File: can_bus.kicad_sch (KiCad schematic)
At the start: 1 part, among them U8 MCP2562-E-SN

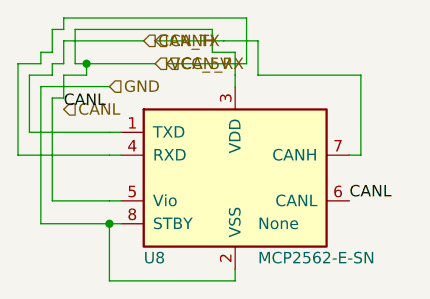
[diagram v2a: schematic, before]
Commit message: optimazed load to kicad
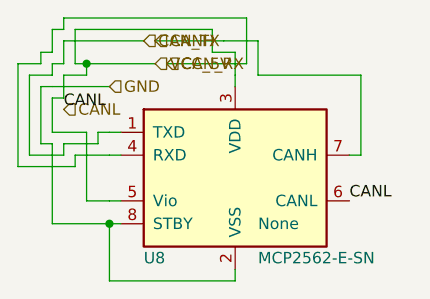
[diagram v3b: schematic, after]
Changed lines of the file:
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@@
 		(instances
 			(project "Untitled"
-				(path "/64cf9334-2063-4cd7-ba0e-d205787c78fb"
+				(path "/deb6734f-8716-41b1-a872-d87713bf0c81"
 					(reference "U8")
 					(unit 1)
@@
 	(wire
 		(pts
-			(xy 21.59 26.67) (xy 15.24 26.67)
-		)
-		(stroke
-			(width 0)
-			(type default)
-		)
-	)
-	(wire
-		(pts
-			(xy 15.24 26.67) (xy 15.24 15.24)
+			(xy 21.59 26.67) (xy 19.05 26.67)
+		)
+		(stroke
+			(width 0)
+			(type default)
+		)
+	)
+	(wire
+		(pts
+			(xy 19.05 26.67) (xy 19.05 19.05)
+		)
+		(stroke
+			(width 0)
+			(type default)
+		)
+	)
+	(wire
+		(pts
+			(xy 19.05 19.05) (xy 15.24 19.05)
+		)
+		(stroke
+			(width 0)
+			(type default)
+		)
+	)
+	(wire
+		(pts
+			(xy 15.24 19.05) (xy 15.24 15.24)
 		)
 		(stroke
@@
 	(wire
 		(pts
-			(xy 21.59 29.21) (xy 13.97 29.21)
-		)
-		(stroke
-			(width 0)
-			(type default)
-		)
-	)
-	(wire
-		(pts
-			(xy 13.97 29.21) (xy 13.97 13.97)
+			(xy 21.59 29.21) (xy 15.24 29.21)
+		)
+		(stroke
+			(width 0)
+			(type default)
+		)
+	)
+	(wire
+		(pts
+			(xy 15.24 29.21) (xy 15.24 20.32)
+		)
+		(stroke
+			(width 0)
+			(type default)
+		)
+	)
+	(wire
+		(pts
+			(xy 15.24 20.32) (xy 13.97 20.32)
+		)
+		(stroke
+			(width 0)
+			(type default)
+		)
+	)
+	(wire
+		(pts
+			(xy 13.97 20.32) (xy 13.97 13.97)
 		)
 		(stroke
@@
 	(wire
 		(pts
-			(xy 21.59 19.05) (xy 12.7 19.05)
-		)
-		(stroke
-			(width 0)
-			(type default)
-		)
-	)
-	(wire
-		(pts
-			(xy 12.7 19.05) (xy 12.7 12.7)
+			(xy 21.59 19.05) (xy 20.32 19.05)
+		)
+		(stroke
+			(width 0)
+			(type default)
+		)
+	)
+	(wire
+		(pts
+			(xy 20.32 19.05) (xy 20.32 20.32)
+		)
+		(stroke
+			(width 0)
+			(type default)
+		)
+	)
+	(wire
+		(pts
+			(xy 20.32 20.32) (xy 16.51 20.32)
+		)
+		(stroke
+			(width 0)
+			(type default)
+		)
+	)
+	(wire
+		(pts
+			(xy 16.51 20.32) (xy 16.51 21.59)
+		)
+		(stroke
+			(width 0)
+			(type default)
+		)
+	)
+	(wire
+		(pts
+			(xy 16.51 21.59) (xy 12.7 21.59)
+		)
+		(stroke
+			(width 0)
+			(type default)
+		)
+	)
+	(wire
+		(pts
+			(xy 12.7 21.59) (xy 12.7 12.7)
 		)
 		(stroke
@@
 	(wire
 		(pts
-			(xy 21.59 21.59) (xy 11.43 21.59)
-		)
-		(stroke
-			(width 0)
-			(type default)
-		)
-	)
-	(wire
-		(pts
-			(xy 11.43 21.59) (xy 11.43 11.43)
-		)
-		(stroke
+			(xy 21.59 21.59) (xy 17.78 21.59)
+		)
+		(stroke
+			(width 0)
+			(type default)
+		)
+	)
+	(wire
+		(pts
+			(xy 17.78 21.59) (xy 17.78 22.86)
+		)
+		(stroke
+			(width 0)
+			(type default)
+		)
+	)
+	(wire
+		(pts
+			(xy 17.78 22.86) (xy 11.43 22.86)
+		)
+		(stroke
+			(width 0)
+			(type default)
+		)
+	)
+	(wire
+		(pts
+			(xy 11.43 22.86) (xy 11.43 11.43)
+		)
+		(stroke

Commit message: tests_fix
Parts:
- U8: hierarchy_path (none) -> /c5a034c1-1f54-4e7e-8711-0930d2b4314e/3e6f426e-0825-4ec4-9e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
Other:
- title: (none) -> climate_control_niva_travel
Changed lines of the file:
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@@
 	(generator_version "9.0")
 	(paper "A4")
+	(title_block
+		(title "climate_control_niva_travel")
+	)
 	(symbol
 		(lib_id "Interface_CAN_LIN:MCP2562-E-SN")
@@
 			)
 		)
+		(property "hierarchy_path" "/c5a034c1-1f54-4e7e-8711-0930d2b4314e/3e6f426e-0825-4ec4-9e13-95c41a6eab89"
+			(at 38.1 29.2099 0)
+			(effects
+				(font
+					(size 1.27 1.27)
+				)
+				(justify left)
+			)
+		)
 		(pin "1"
 		)
@@
 		)
 		(instances
-			(project "Untitled"
-				(path "/deb6734f-8716-41b1-a872-d87713bf0c81"
+			(project "climate_control_niva_travel"
+				(path "/c5a034c1-1f54-4e7e-8711-0930d2b4314e/3e6f426e-0825-4ec4-9e13-95c41a6eab89"
 					(reference "U8")
 					(unit 1)
@@
 	)
 	(hierarchical_label "CAN_RX"
-		(shape input)
+		(shape output)
 		(at 27.94 11.43 0)
 		(effects
@@
 	)
 	(hierarchical_label "CANH"
-		(shape input)
+		(shape output)
 		(at 26.67 8.89 0)
 		(effects
@@
 	)
 	(hierarchical_label "CANL"
-		(shape input)
+		(shape output)
 		(at 16.51 16.51 0)
 		(effects

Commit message: refactoring
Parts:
- U8: hierarchy_path /c5a034c1-1f54-4e7e-8711-0930d2b4314e/3e6f426e-0825-4ec4-9e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 -> (none)
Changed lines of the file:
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@@
-			)
-		)
-		(property "hierarchy_path" "/c5a034c1-1f54-4e7e-8711-0930d2b4314e/3e6f426e-0825-4ec4-9e13-95c41a6eab89"
-			(at 38.1 29.2099 0)
-			(effects
-				(font
-					(size 1.27 1.27)
-				)
-				(justify left)
 			)
 		)
@@
 		(instances
 			(project "climate_control_niva_travel"
-				(path "/c5a034c1-1f54-4e7e-8711-0930d2b4314e/3e6f426e-0825-4ec4-9e13-95c41a6eab89"
-					(reference "U8")
+				(path "/165a98f1-2dde-4141-9fdc-c935d39c8cff/07ec9d0b-cd95-49f4-92c1-d02e79bd1c75/"
+					(reference "U0808")
 					(unit 1)
 				)

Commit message: refactoring
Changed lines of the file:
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@@
+			)
+		)
+		(property "Sim.Device" "X"
+			(at 38.1 29.2099 0)
+			(effects
+				(font
+					(size 1.27 1.27)
+				)
+				(justify left)
+			)
+		)
+		(property "Sim.Name" "MCP2562"
+			(at 38.1 29.2099 0)
+			(effects
+				(font
+					(size 1.27 1.27)
+				)
+				(justify left)
+			)
+		)
+		(property "Sim.Library" "${KIPRJMOD}/spice/lib/mcp2562_ngspice.lib"
+			(at 38.1 29.2099 0)
+			(effects
+				(font
+					(size 1.27 1.27)
+				)
+				(justify left)
+			)
+		)
+		(property "Sim.Pins" "1=TXD 4=RXD 7=CANH 6=CANL 8=STBY 3=VDD 5=VIO 2=GND"
+			(at 38.1 29.2099 0)
+			(effects
+				(font
+					(size 1.27 1.27)
+				)
+				(justify left)
+			)
+		)
+		(property "Sim.Enable" "1"
+			(at 38.1 29.2099 0)
+			(effects
+				(font
+					(size 1.27 1.27)
+				)
+				(justify left)
 			)
 		)
@@
 		(instances
 			(project "climate_control_niva_travel"
-				(path "/165a98f1-2dde-4141-9fdc-c935d39c8cff/07ec9d0b-cd95-49f4-92c1-d02e79bd1c75/"
+				(path "/cc416b40-1361-4232-ac1e-5cd36ef0c0fb/c39f5ba4-c7f2-413a-b1c4-1fa4d87e42a0/"
 					(reference "U0808")
 					(unit 1)
@@
 	(junction
 		(at 19.05 11.43)
-		(diameter 0)
+		(diameter 0.0000)
 		(color 0 0 0 0)
 	)
 	(junction
 		(at 21.59 29.21)
-		(diameter 0)
+		(diameter 0.0000)
 		(color 0 0 0 0)
 	)
